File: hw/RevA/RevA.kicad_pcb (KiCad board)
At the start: 4 copper layers, 100 x 60 mm, 112 parts, among them CON1 N64-Cartridge, J1 USB_C_Receptacle_USB2.0, J2 Micro_SD_Card, J3 DNP Conn_01x02, SW1 SW_Push, U1 SY8120B1ABC, U2 XC6206P25, U3 SY8120B1ABC, U4 SPI Flash W25Q128JVSIQ, U6 IS42S16320F-7TL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

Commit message: WIP
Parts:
- moved JP1 9.88 mm to (110.5, 81.0), turned to 180 degrees
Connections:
- JP1 pad 1: VBUS -> +12V
- JP1 pad 3: +12V -> VBUS
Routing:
- net Net-(FB1-Pad1): track 13.6 -> 10.2 mm
- net VBUS: track 18.6 -> 21.4 mm
- net +12V: track 93.0 -> 95.0 mm

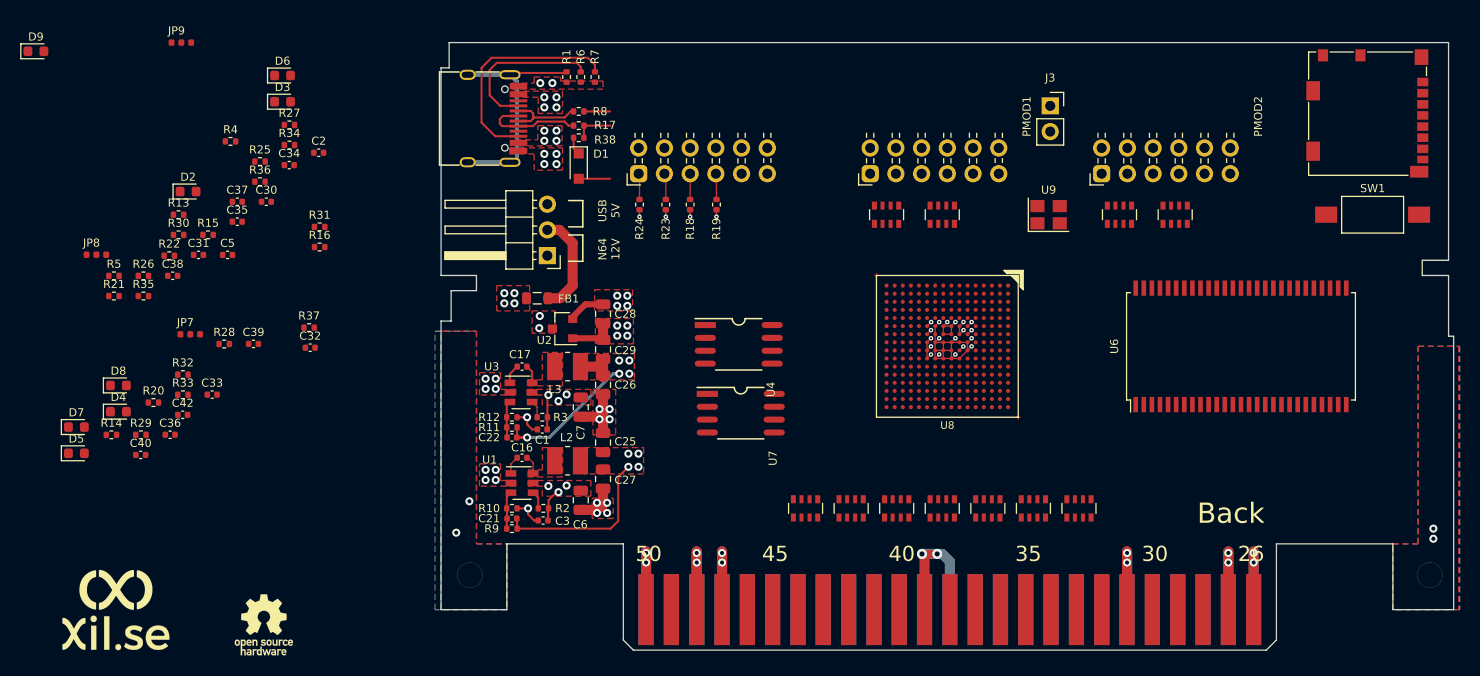
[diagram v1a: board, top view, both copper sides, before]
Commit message: hw: Progress
- Added pullup resistor for CIC data
- Removed extra SPI flash (no need for it anymore)
- Rounded corners
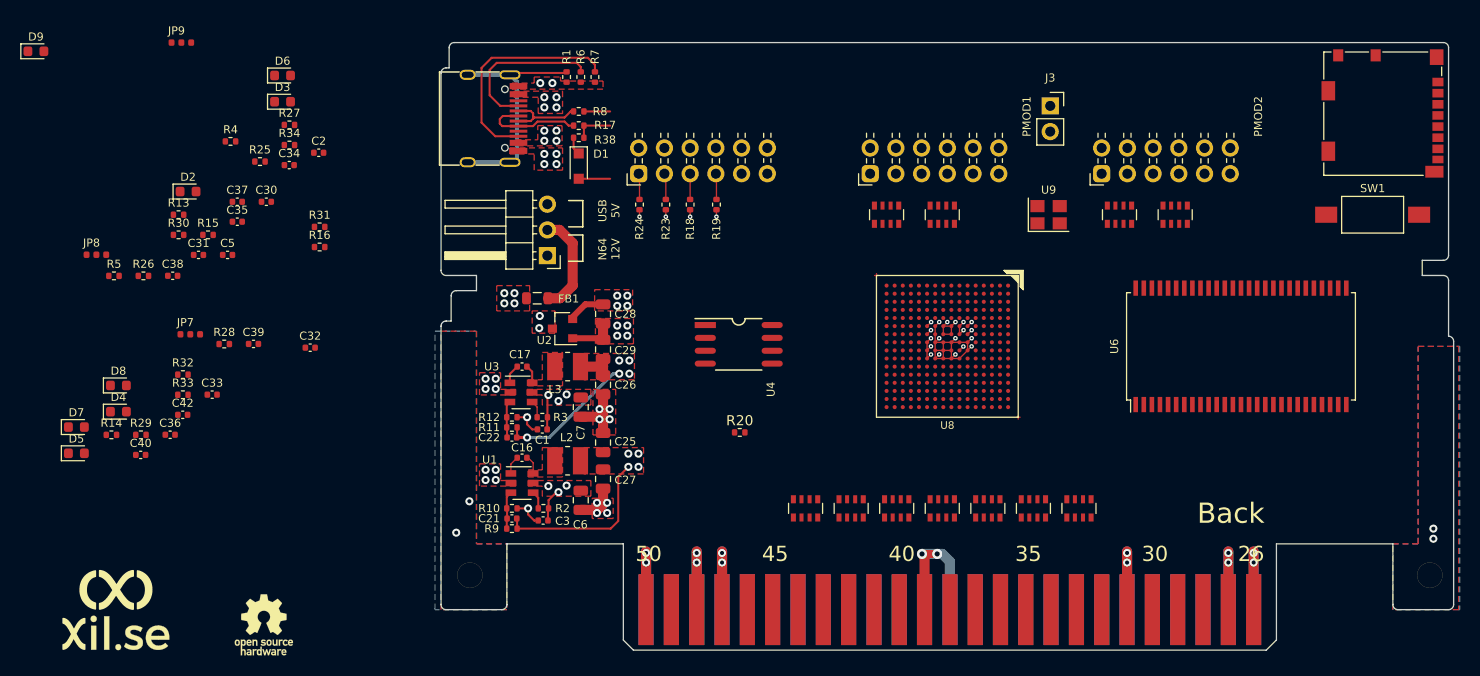
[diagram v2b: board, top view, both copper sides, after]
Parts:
- removed R21: 4K7, Resistor_SMD:R_0402_1005Metric
- removed R22, R35, R36, R37: 10K, Resistor_SMD:R_0402_1005Metric
- removed U7: SPI Flash W25Q128JVSIQ, ecp5board:SOA008-150-208mil
- R20: value 1K -> 10K
- moved R20 58.0 mm to (129.5, 98.5)
- moved J2 1.50 mm to (193.0, 67.0)
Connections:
- net Net-(CON1-Pad44) renamed /N64_INT1
- R20 pad 1: /FPGA_SPI2_CLK -> /N64_CIC_DIO
- R20 pad 2: +3V3 -> Net-(R20-Pad2)
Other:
- outline, holes or cut-outs redrawn
